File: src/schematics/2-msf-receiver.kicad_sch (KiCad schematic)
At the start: 69 parts, among them U201 TPS7A2040PDQNR, U202 TPS7A2036PDBVR, U203 MCP6499, U204 MCP6499, U205 74HC595BQ

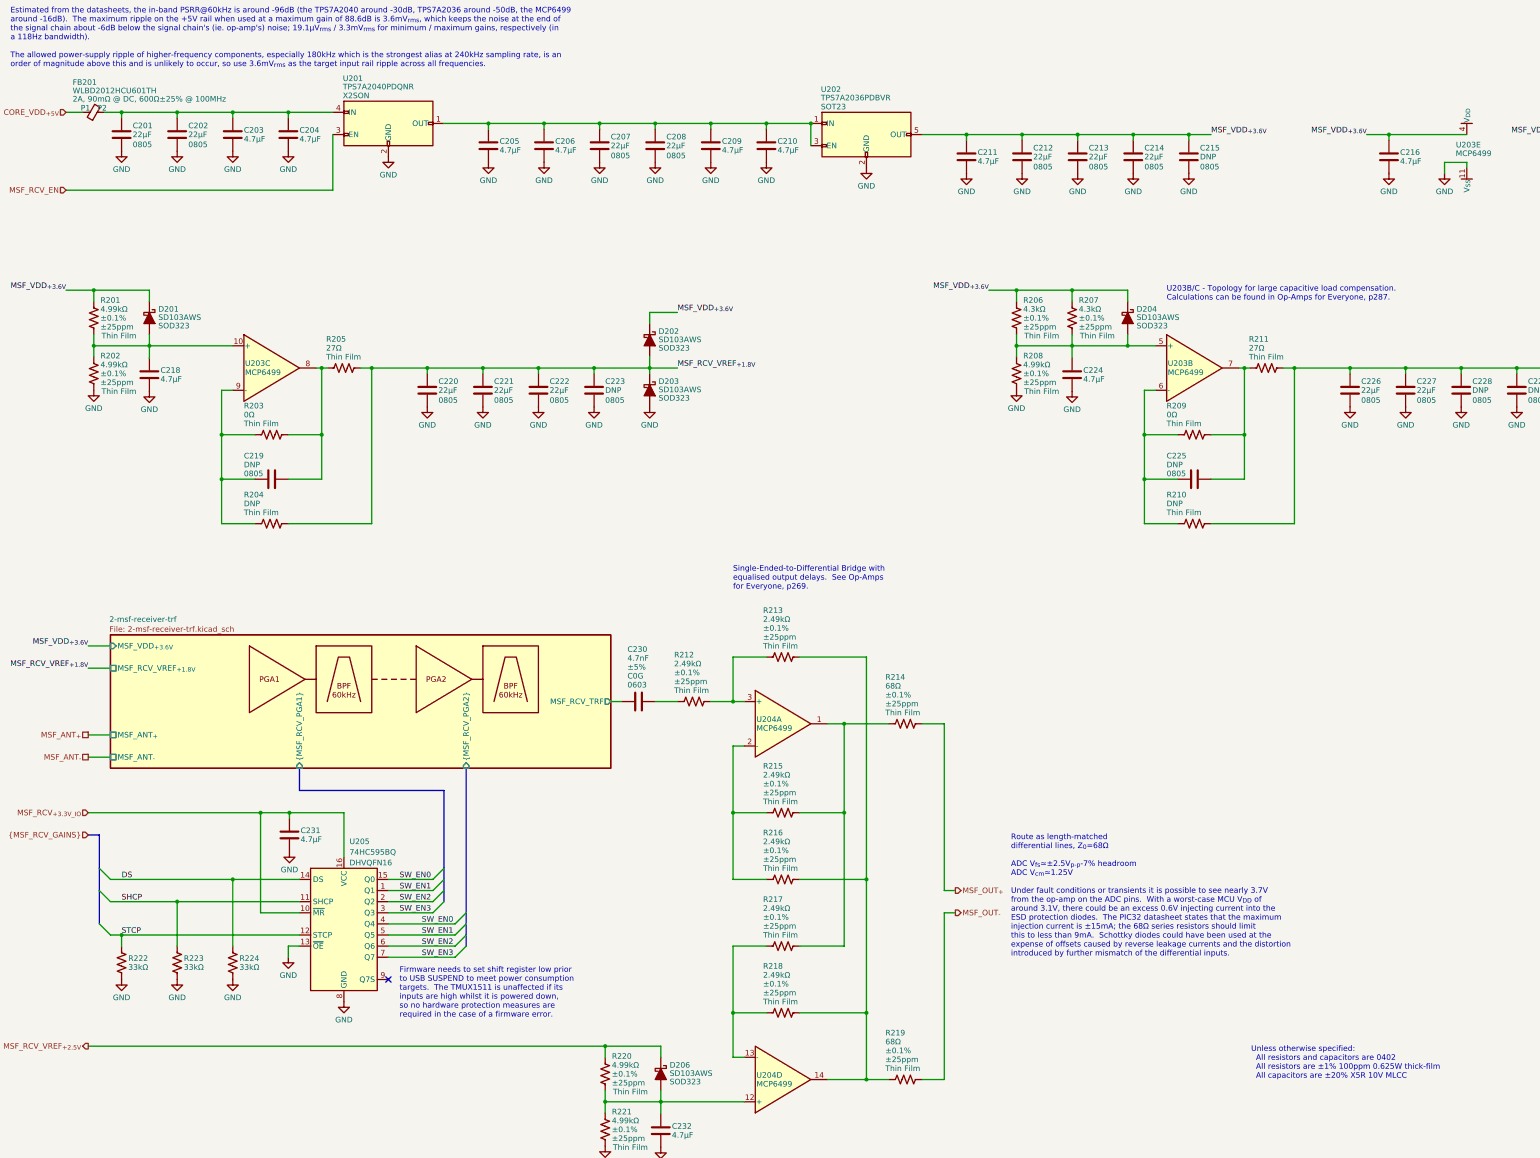
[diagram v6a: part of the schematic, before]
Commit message: Various tidy-ups and checks, mainly around the bypass capacitors.  Added a load of test points.
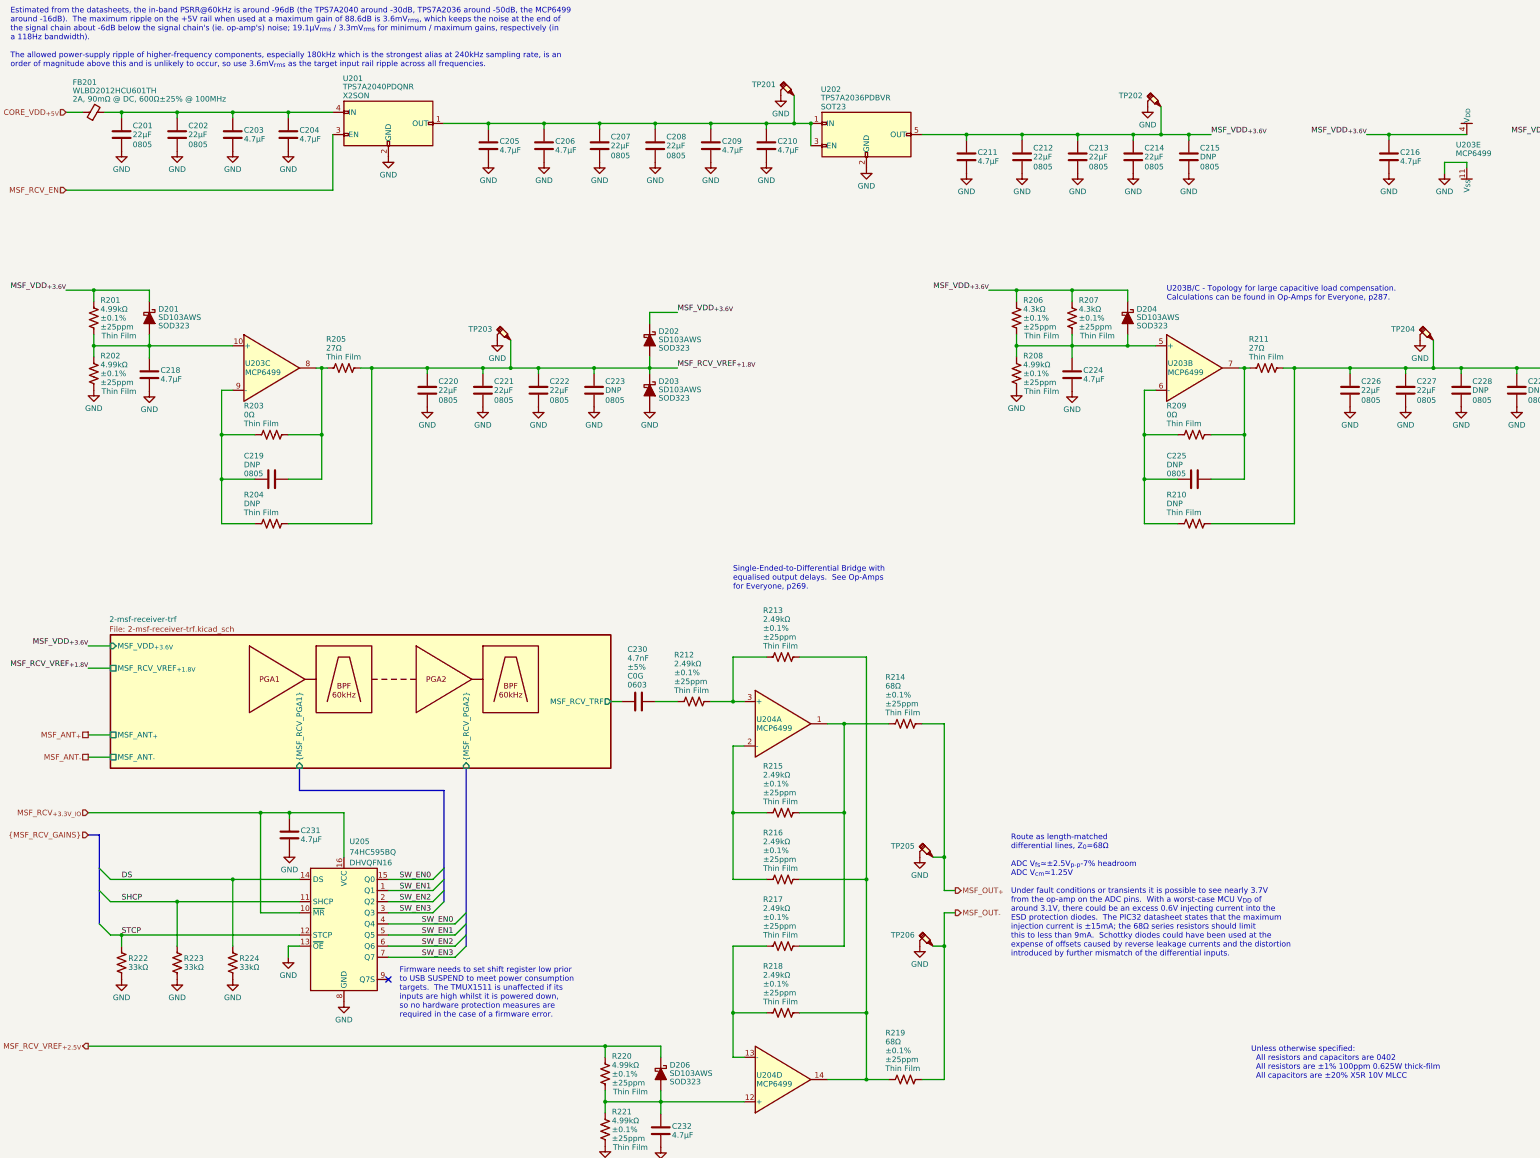
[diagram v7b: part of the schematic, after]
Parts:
- added TP201, TP202, TP203, TP204, TP205, TP206: ~, restall-generic-test:testpoint-SP3050A-with-short-gnd, symbol restall-generic-test:testpoint-probe-with-gnd
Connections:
- net GND: now also TP201.2 (GND), TP202.2 (GND), TP203.2 (GND), TP204.2 (GND), TP205.2 (GND), TP206.2 (GND)
- net MSF_OUT_{+}: now also TP205.1
- net MSF_OUT_{-}: now also TP206.1
- net MSF_RCV_VREF_{+1.8V}: now also TP203.1
- net MSF_RCV_VREF_{+2.5V}: now also TP204.1
- net MSF_VDD_{+3.6V}: now also TP202.1
- net at C205.1, C206.1, C207.1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: now also TP201.1

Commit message: Added part numbers for the capacitors.
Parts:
- C203, C204, C205, C206, C209, C210, C211, C216, C217, C218, C224, C231, C232: ManufacturerPartNumber (none) -> CL05A475MP5NRNC
- FB201: Package (none) -> WLBD2012
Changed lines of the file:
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@@
       (effects (font (size 1.27 1.27)) (justify left) hide)
     )
-    (property "ManufacturerPartNumber" "" (at 378.46 50.8 0)
+    (property "ManufacturerPartNumber" "CL05A475MP5NRNC" (at 378.46 50.8 0)
       (effects (font (size 1.27 1.27)) (justify left) hide)
     )
@@
       (effects (font (size 1.27 1.27)) (justify left) hide)
     )
-    (property "ManufacturerPartNumber" "" (at 68.58 45.72 0)
+    (property "ManufacturerPartNumber" "CL05A475MP5NRNC" (at 68.58 45.72 0)
       (effects (font (size 1.27 1.27)) (justify left) hide)
     )
@@
       (effects (font (size 1.27 1.27)) (justify left) hide)
     )
-    (property "ManufacturerPartNumber" "" (at 190.5 48.26 0)
+    (property "ManufacturerPartNumber" "CL05A475MP5NRNC" (at 190.5 48.26 0)
       (effects (font (size 1.27 1.27)) (justify left) hide)
     )
@@
       (effects (font (size 1.27 1.27)) (justify left) hide)
     )
-    (property "ManufacturerPartNumber" "" (at 81.534 205.74 0)
+    (property "ManufacturerPartNumber" "CL05A475MP5NRNC" (at 81.534 205.74 0)
       (effects (font (size 1.27 1.27)) (justify left) hide)
     )
@@
       (effects (font (size 1.27 1.27)) (justify left) hide)
     )
-    (property "ManufacturerPartNumber" "" (at 332.74 50.8 0)
+    (property "ManufacturerPartNumber" "CL05A475MP5NRNC" (at 332.74 50.8 0)
       (effects (font (size 1.27 1.27)) (justify left) hide)
     )
@@
       (effects (font (size 1.27 1.27)) (justify left) hide)
     )
-    (property "ManufacturerPartNumber" "" (at 81.28 45.72 0)
+    (property "ManufacturerPartNumber" "CL05A475MP5NRNC" (at 81.28 45.72 0)
       (effects (font (size 1.27 1.27)) (justify left) hide)
     )
@@
       (effects (font (size 1.27 1.27)) (justify left) hide)
     )
-    (property "ManufacturerPartNumber" "" (at 127 48.26 0)
+    (property "ManufacturerPartNumber" "CL05A475MP5NRNC" (at 127 48.26 0)
       (effects (font (size 1.27 1.27)) (justify left) hide)
     )
@@
       (effects (font (size 1.27 1.27)) (justify left) hide)
     )
-    (property "ManufacturerPartNumber" "" (at 236.22 50.8 0)
+    (property "ManufacturerPartNumber" "CL05A475MP5NRNC" (at 236.22 50.8 0)
       (effects (font (size 1.27 1.27)) (justify left) hide)
     )
@@
       (effects (font (size 1.27 1.27)) (justify left) hide)
     )
-    (property "ManufacturerPartNumber" "" (at 139.7 48.26 0)
+    (property "ManufacturerPartNumber" "CL05A475MP5NRNC" (at 139.7 48.26 0)
       (effects (font (size 1.27 1.27)) (justify left) hide)
     )
@@
       (effects (font (size 1.27 1.27)) (justify left) hide)
     )
+    (property "Package" "WLBD2012" (at 36.83 40.64 0)
+      (effects (font (size 1.27 1.27)) hide)
+    )
     (pin "1")
     (pin "2")
@@
       (effects (font (size 1.27 1.27)) (justify left) hide)
     )
-    (property "ManufacturerPartNumber" "" (at 177.8 48.26 0)
+    (property "ManufacturerPartNumber" "CL05A475MP5NRNC" (at 177.8 48.26 0)
       (effects (font (size 1.27 1.27)) (justify left) hide)
     )
@@
       (effects (font (size 1.27 1.27)) (justify left) hide)
     )
-    (property "ManufacturerPartNumber" "" (at 49.53 100.584 0)
+    (property "ManufacturerPartNumber" "CL05A475MP5NRNC" (at 49.53 100.584 0)
       (effects (font (size 1.27 1.27)) (justify left) hide)
     )
@@
       (effects (font (size 1.27 1.27)) (justify left) hide)
     )
-    (property "ManufacturerPartNumber" "" (at 260.35 100.584 0)
+    (property "ManufacturerPartNumber" "CL05A475MP5NRNC" (at 260.35 100.584 0)
       (effects (font (size 1.27 1.27)) (justify left) hide)
     )
@@
       (effects (font (size 1.27 1.27)) (justify left) hide)
     )
-    (property "ManufacturerPartNumber" "" (at 166.37 273.304 0)
+    (property "ManufacturerPartNumber" "CL05A475MP5NRNC" (at 166.37 273.304 0)
       (effects (font (size 1.27 1.27)) (justify left) hide)
     )
